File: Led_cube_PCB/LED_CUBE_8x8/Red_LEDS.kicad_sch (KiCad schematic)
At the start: 34 parts, among them IC16 74AHCT244PW,118, IC19 74AHCT244PW,118, IC20 74AHCT244PW,118, IC21 74AHCT244PW,118, IC22 74AHCT244PW,118, IC4 74AHCT244PW,118, IC5 74AHCT244PW,118, IC6 74AHCT244PW,118, IC7 74AHC138PW,118

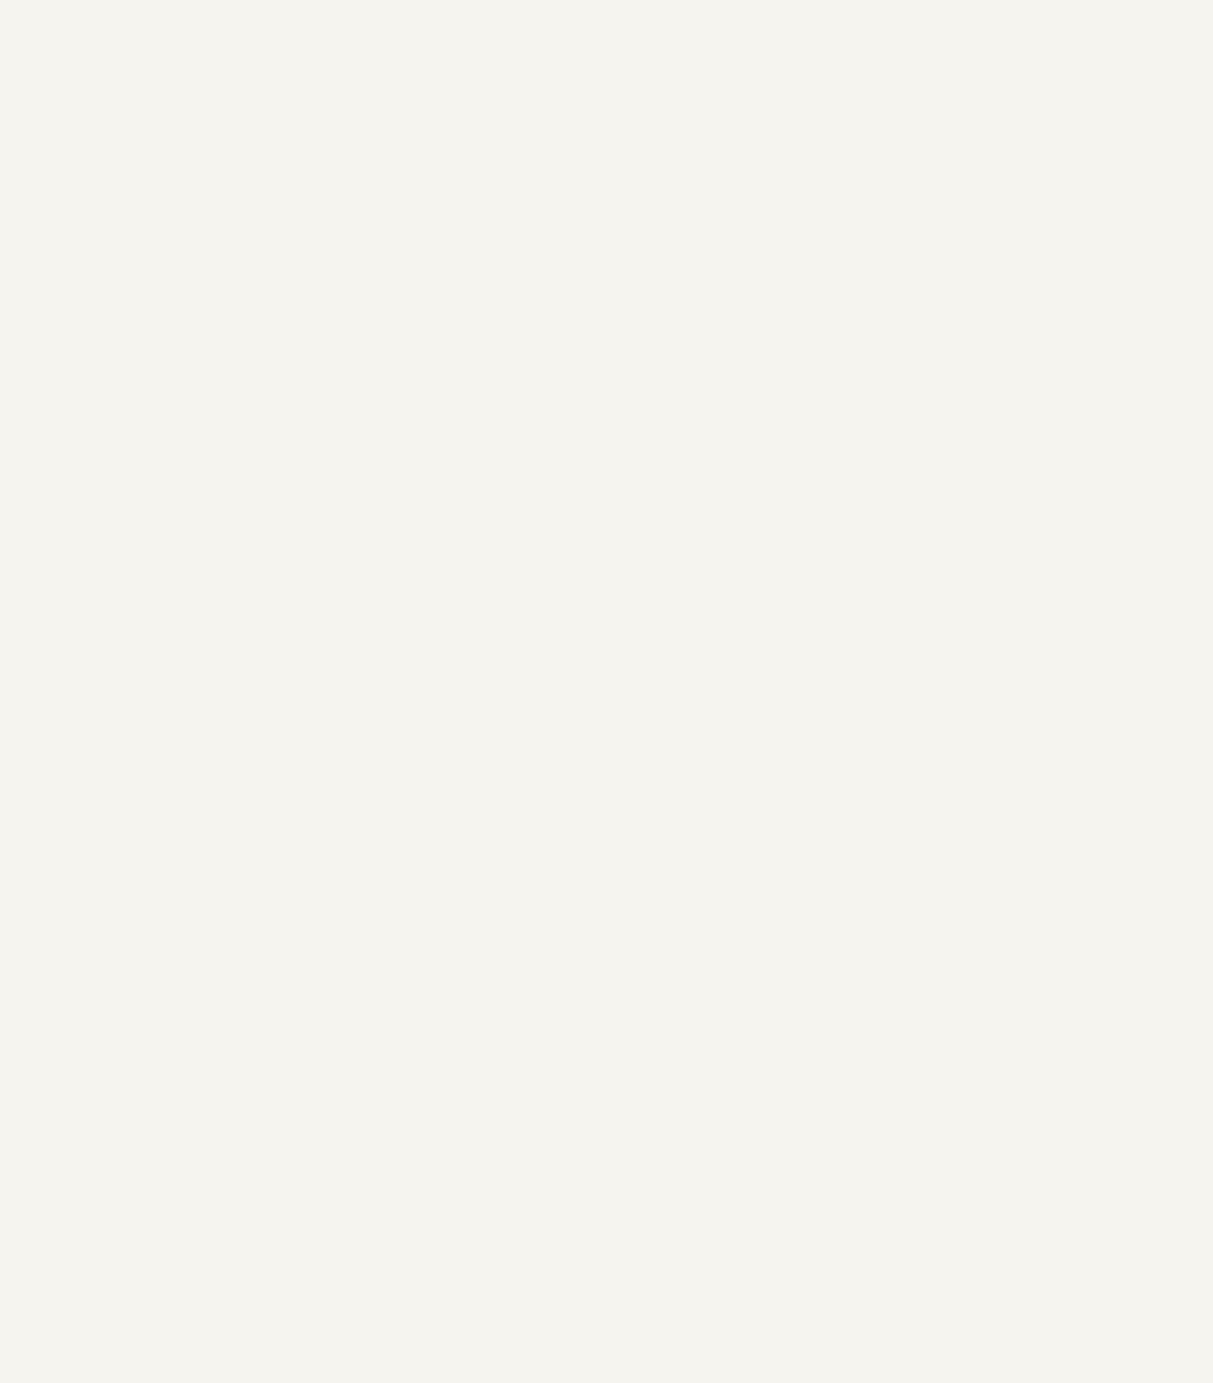
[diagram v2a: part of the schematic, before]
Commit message: added connector and current limiting resistors of the RED channel.
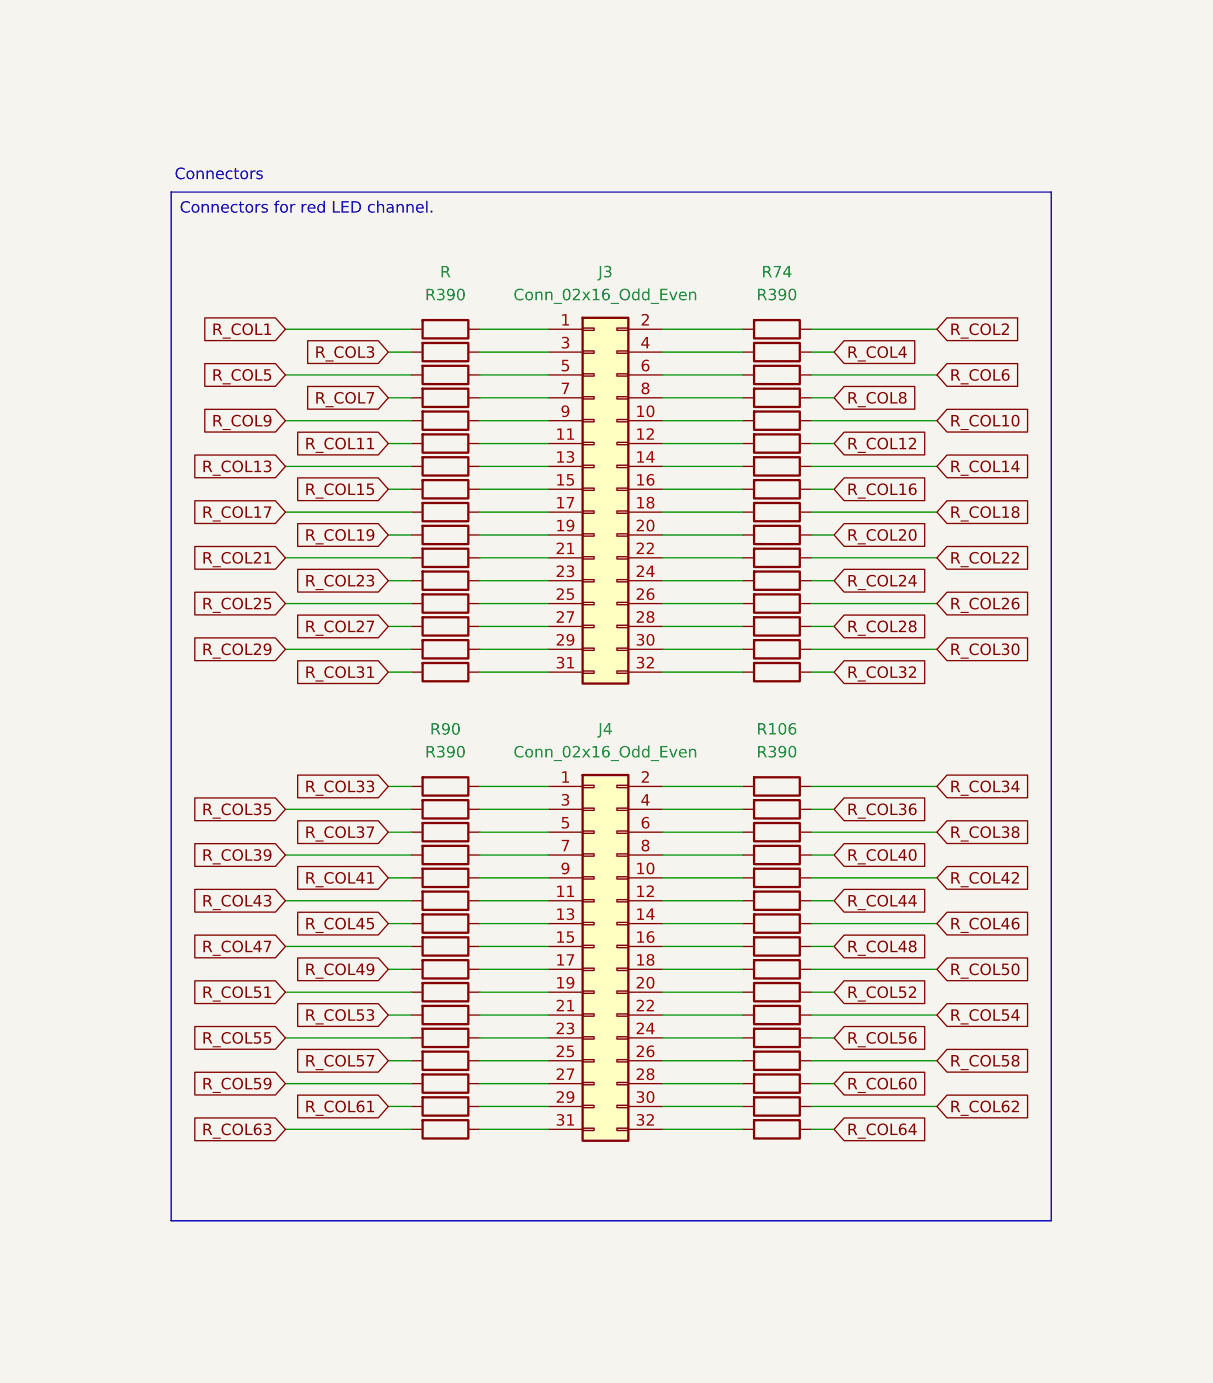
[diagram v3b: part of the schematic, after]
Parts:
- added J3, J4: Conn_02x16_Odd_Even, Connector_PinHeader_1.00mm:PinHeader_2x16_P1.00mm_Vertical, symbol Connector_Generic:Conn_02x16_Odd_Even
- added R (x2), R100, R101, R102, R103, R104, R105, R106, R107, R108, R109, R110, R111, R112, R113, R114, R115, R116, R117, R118, R119, R120, R121, R60, R61, R62, R63, R64, R65, R66, R67, R68, R69, R70, R71, R72, R73, R74, R75, R76, R77, R78, R79, R80, R81, R82, R83, R84, R85, R86, R87, R88, R89, R90, R91, R92, R93, R94, R95, R96, R97, R98, R99: R390, symbol Device:R
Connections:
- net R_COL1: now also R.2
- net R_COL10: now also R78.1
- net R_COL11: now also R63.2
- net R_COL12: now also R79.1
- net R_COL13: now also R64.2
- net R_COL14: now also R80.1
- net R_COL15: now also R65.2
- net R_COL16: now also R81.1
- net R_COL17: now also R66.2
- net R_COL18: now also R82.1
- net R_COL19: now also R67.2
- net R_COL2: now also R74.1
- net R_COL20: now also R83.1
- net R_COL21: now also R68.2
- net R_COL22: now also R84.1
- net R_COL23: now also R69.2
- net R_COL24: now also R85.1
- net R_COL25: now also R70.2
- net R_COL26: now also R86.1
- net R_COL27: now also R71.2
- net R_COL28: now also R87.1
- net R_COL29: now also R72.2
- net R_COL3: now also R.2
- net R_COL30: now also R88.1
- net R_COL31: now also R73.2
- net R_COL32: now also R89.1
- net R_COL33: now also R90.2
- net R_COL34: now also R106.1
- net R_COL35: now also R91.2
- net R_COL36: now also R107.1
- net R_COL37: now also R92.2
- net R_COL38: now also R108.1
- net R_COL39: now also R93.2
- net R_COL4: now also R75.1
- net R_COL40: now also R109.1
- net R_COL41: now also R94.2
- net R_COL42: now also R110.1
- net R_COL43: now also R95.2
- net R_COL44: now also R111.1
- net R_COL45: now also R96.2
- net R_COL46: now also R112.1
- net R_COL47: now also R97.2
- net R_COL48: now also R113.1
- net R_COL49: now also R98.2
- net R_COL5: now also R60.2
- net R_COL50: now also R114.1
- net R_COL51: now also R99.2
- net R_COL52: now also R115.1
- net R_COL53: now also R100.2
- net R_COL54: now also R116.1
- net R_COL55: now also R101.2
- net R_COL56: now also R117.1
- net R_COL57: now also R102.2
- net R_COL58: now also R118.1
- net R_COL59: now also R103.2
- net R_COL6: now also R76.1
- net R_COL60: now also R119.1
- net R_COL61: now also R104.2
- net R_COL62: now also R120.1
- net R_COL63: now also R105.2
- net R_COL64: now also R121.1
- net R_COL7: now also R61.2
- net R_COL8: now also R77.1
- net R_COL9: now also R62.2
- new net: J3.24 (Pin_24), R85.2
- new net: J3.32 (Pin_32), R89.2
- new net: J3.26 (Pin_26), R86.2
- new net: J4.11 (Pin_11), R95.1
- new net: J3.28 (Pin_28), R87.2
- new net: J4.16 (Pin_16), R113.2
- new net: J4.24 (Pin_24), R117.2
- new net: J4.29 (Pin_29), R104.1
- new net: J3.25 (Pin_25), R70.1
- new net: J4.26 (Pin_26), R118.2
- new net: J4.25 (Pin_25), R102.1
- new net: J4.23 (Pin_23), R101.1
- new net: J4.6 (Pin_6), R108.2
- new net: J3.20 (Pin_20), R83.2
- new net: J3.19 (Pin_19), R67.1
- new net: J3.14 (Pin_14), R80.2
- new net: J3.7 (Pin_7), R61.1
- new net: J4.10 (Pin_10), R110.2
- new net: J3.2 (Pin_2), R74.2
- new net: J4.32 (Pin_32), R121.2
- new net: J3.6 (Pin_6), R76.2
- new net: J4.9 (Pin_9), R94.1
- new net: J4.22 (Pin_22), R116.2
- new net: J4.27 (Pin_27), R103.1
- new net: J3.5 (Pin_5), R60.1
- new net: J3.10 (Pin_10), R78.2
- new net: J4.31 (Pin_31), R105.1
- new net: J4.3 (Pin_3), R91.1
- new net: J4.18 (Pin_18), R114.2
- new net: J3.22 (Pin_22), R84.2
- new net: J4.12 (Pin_12), R111.2
- new net: J4.17 (Pin_17), R98.1
- new net: J3.18 (Pin_18), R82.2
- new net: J3.9 (Pin_9), R62.1
- new net: J4.7 (Pin_7), R93.1
- new net: J3.15 (Pin_15), R65.1
- new net: J3.1 (Pin_1), R.1
- new net: J4.4 (Pin_4), R107.2
- new net: J3.21 (Pin_21), R68.1
- new net: J3.4 (Pin_4), R75.2
- new net: J3.8 (Pin_8), R77.2
- new net: J4.30 (Pin_30), R120.2
- new net: J3.11 (Pin_11), R63.1
- new net: J3.12 (Pin_12), R79.2
- new net: J3.13 (Pin_13), R64.1
- new net: J3.16 (Pin_16), R81.2
- new net: J3.17 (Pin_17), R66.1
- new net: J3.23 (Pin_23), R69.1
- new net: J3.27 (Pin_27), R71.1
- new net: J3.29 (Pin_29), R72.1
- new net: J3.3 (Pin_3), R.1
- new net: J3.30 (Pin_30), R88.2
- new net: J3.31 (Pin_31), R73.1
- new net: J4.15 (Pin_15), R97.1
- new net: J4.1 (Pin_1), R90.1
- new net: J4.13 (Pin_13), R96.1
- new net: J4.14 (Pin_14), R112.2
- new net: J4.19 (Pin_19), R99.1
- new net: J4.2 (Pin_2), R106.2
- new net: J4.20 (Pin_20), R115.2
- new net: J4.21 (Pin_21), R100.1
- new net: J4.28 (Pin_28), R119.2
- new net: J4.5 (Pin_5), R92.1
- new net: J4.8 (Pin_8), R109.2
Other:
- note added: "Connectors"

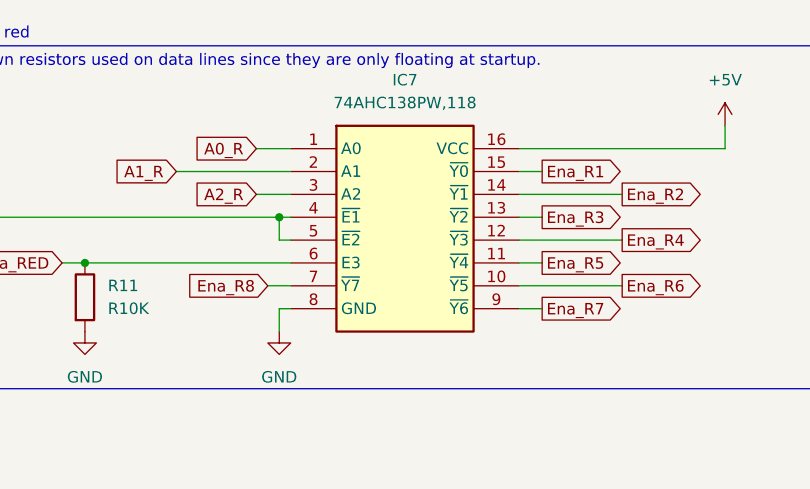
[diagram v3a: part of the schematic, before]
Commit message: added spice simulations folder, For simulating transients effect on the power buck converter. Also finished layer select in eeschema.
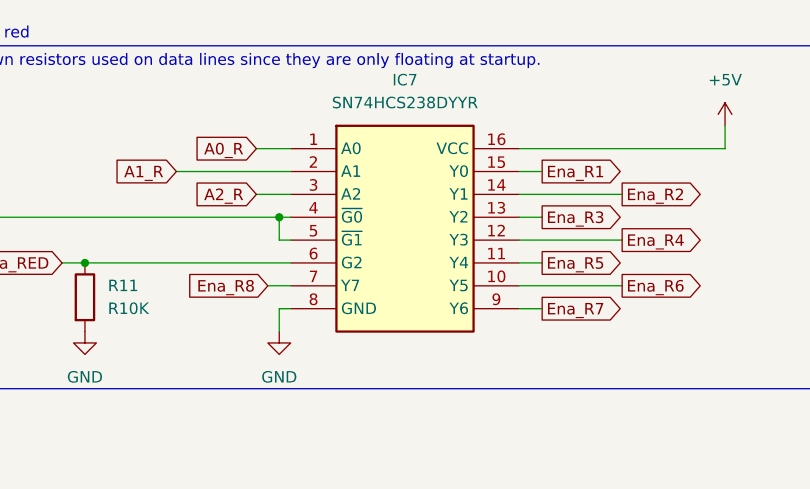
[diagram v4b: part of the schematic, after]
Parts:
- removed IC7: 74AHC138PW,118, SOP65P640X110-16N, symbol SamacSys_Parts:74AHC138PW,118
- added IC7: SN74HCS238DYYR, SOP50P326X110-16N, symbol SamacSys_Parts:SN74HCS238DYYR
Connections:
- net +5V: now also IC7.16 (VCC)
- net A0_R: now also IC7.1 (A0)
- net A1_R: now also IC7.2 (A1)
- net A2_R: now also IC7.3 (A2)
- net Ena_R1: now also IC7.15 (Y0)
- net Ena_R2: now also IC7.14 (Y1)
- net Ena_R3: now also IC7.13 (Y2)
- net Ena_R4: now also IC7.12 (Y3)
- net Ena_R5: now also IC7.11 (Y4)
- net Ena_R6: now also IC7.10 (Y5)
- net Ena_R7: now also IC7.9 (Y6)
- net Ena_R8: now also IC7.7 (Y7)
- net Ena_RED: now also IC7.6 (G2)
- net GND: now also IC7.4 (~{G0}), IC7.5 (~{G1}), IC7.8 (GND)
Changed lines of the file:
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@@
 	)
 	(symbol
+		(lib_id "SamacSys_Parts:SN74HCS238DYYR")
+		(at 335.28 27.94 0)
+		(unit 1)
+		(exclude_from_sim no)
+		(in_bom yes)
+		(on_board yes)
+		(dnp no)
+		(fields_autoplaced yes)
+		(property "Reference" "IC7"
+			(at 347.98 20.32 0)
+			(effects
+				(font
+					(size 1.27 1.27)
+				)
+			)
+		)
+		(property "Value" "SN74HCS238DYYR"
+			(at 347.98 22.86 0)
+			(effects
+				(font
+					(size 1.27 1.27)
+				)
+			)
+		)
+		(property "Footprint" "SOP50P326X110-16N"
+			(at 356.87 122.86 0)
+			(effects
+				(font
+					(size 1.27 1.27)
+				)
+				(justify left top)
+				(hide yes)
+			)
+		)
+		(property "Datasheet" "https://www.ti.com/general/docs/suppproductinfo.tsp?distId=26&gotoUrl=https://www.ti.com/lit/gpn/sn74hcs238"
+			(at 356.87 222.86 0)
+			(effects
+				(font
+					(size 1.27 1.27)
+				)
+				(justify left top)
+				(hide yes)
+			)
+		)
+		(property "Description" "3-To-8 Line Decoder Demultiplexer Inverting And Non-Inverting With Schmitt-Trigger Input"
+			(at 335.28 27.94 0)
+			(effects
+				(font
+					(size 1.27 1.27)
+				)
+				(hide yes)
+			)
+		)
+		(property "Height" "1.1"
+			(at 356.87 422.86 0)
+			(effects
+				(font
+					(size 1.27 1.27)
+				)
+				(justify left top)
+				(hide yes)
+			)
+		)
+		(property "Mouser Part Number" "595-SN74HCS238DYYR"
+			(at 356.87 522.86 0)
+			(effects
+				(font
+					(size 1.27 1.27)
+				)
+				(justify left top)
+				(hide yes)
+			)
+		)
+		(property "Mouser Price/Stock" "https://www.mouser.co.uk/ProductDetail/Texas-Instruments/SN74HCS238DYYR?qs=QNEnbhJQKvaif85BFm1rOg%3D%3D"
+			(at 356.87 622.86 0)
+			(effects
+				(font
+					(size 1.27 1.27)
+				)
+				(justify left top)
+				(hide yes)
+			)
+		)
+		(property "Manufacturer_Name" "Texas Instruments"
+			(at 356.87 722.86 0)
+			(effects
+				(font
+					(size 1.27 1.27)
+				)
+				(justify left top)
+				(hide yes)
+			)
+		)
+		(property "Manufacturer_Part_Number" "SN74HCS238DYYR"
+			(at 356.87 822.86 0)
+			(effects
+				(font
+					(size 1.27 1.27)
+				)
+				(justify left top)
+				(hide yes)
+			)
+		)
+		(pin "13"
+		)
+		(pin "6"
+		)
+		(pin "7"
+		)
+		(pin "4"
+		)
+		(pin "16"
+		)
+		(pin "2"
+		)
+		(pin "1"
+		)
+		(pin "9"
+		)
+		(pin "8"
+		)
+		(pin "3"
+		)
+		(pin "15"
+		)
+		(pin "14"
+		)
+		(pin "12"
+		)
+		(pin "11"
+		)
+		(pin "5"
+		)
+		(pin "10"
+		)
+		(instances
+			(project ""
+				(path "/b239677e-e361-4439-8200-63fb41f7e03c/39f84ab9-cf03-4ef5-a6b6-c3023701b456"
+					(reference "IC7")
+					(unit 1)
+				)
+			)
+		)
+	)
+	(symbol
 		(lib_id "Device:R")
 		(at 355.6 123.19 270)
@@
 					(unit 1)
 				)
-			)
-		)
-	)
-	(symbol
-		(lib_id "SamacSys_Parts:74AHC138PW,118")
-		(at 335.28 27.94 0)
-		(unit 1)
-		(exclude_from_sim no)
-		(in_bom yes)
-		(on_board yes)
-		(dnp no)
-		(fields_autoplaced yes)
-		(property "Reference" "IC7"
-			(at 347.98 20.32 0)
-			(effects
-				(font
-					(size 1.27 1.27)
-				)
-			)
-		)
-		(property "Value" "74AHC138PW,118"
-			(at 347.98 22.86 0)
-			(effects
-				(font
-					(size 1.27 1.27)
-				)
-			)
-		)
-		(property "Footprint" "SOP65P640X110-16N"
-			(at 356.87 122.86 0)
-			(effects
-				(font
-					(size 1.27 1.27)
-				)
-				(justify left top)
-				(hide yes)
-			)
-		)
-		(property "Datasheet" "https://componentsearchengine.com/Datasheets/1/74AHC138PW,118.pdf"
-			(at 356.87 222.86 0)
-			(effects
-				(font
-					(size 1.27 1.27)
-				)
-				(justify left top)
-				(hide yes)
-			)
-		)
-		(property "Description" "74AHC(T)138 - 3-to-8 line decoder/demultiplexer; inverting@en-us"
-			(at 335.28 27.94 0)
-			(effects
-				(font
-					(size 1.27 1.27)
-				)
-				(hide yes)
-			)
-		)
-		(property "Height" "1.1"
-			(at 356.87 422.86 0)
-			(effects
-				(font
-					(size 1.27 1.27)
-				)
-				(justify left top)
-				(hide yes)
-			)
-		)
-		(property "Mouser Part Number" "771-AHC138PW118"
-			(at 356.87 522.86 0)
-			(effects
-				(font
-					(size 1.27 1.27)
-				)
-				(justify left top)
-				(hide yes)
-			)
-		)
-		(property "Mouser Price/Stock" "https://www.mouser.com/Search/Refine.aspx?Keyword=771-AHC138PW118"
-			(at 356.87 622.86 0)
-			(effects
-				(font
-					(size 1.27 1.27)
-				)
-				(justify left top)
-				(hide yes)
-			)
-		)
-		(property "Manufacturer_Name" "Nexperia"
-			(at 356.87 722.86 0)
-			(effects
-				(font
-					(size 1.27 1.27)
-				)
-				(justify left top)
-				(hide yes)
-			)
-		)
-		(property "Manufacturer_Part_Number" "74AHC138PW,118"
-			(at 356.87 822.86 0)
-			(effects
-				(font
-					(size 1.27 1.27)
-				)
-				(justify left top)
-				(hide yes)
-			)
-		)
-		(pin "4"
-		)
-		(pin "15"
-		)
-		(pin "2"
-		)
-		(pin "7"
-		)
-		(pin "12"
-		)
-		(pin "1"
-		)
-		(pin "11"
-		)
-		(pin "10"
-		)
-		(pin "8"
-		)
-		(pin "16"
-		)
-		(pin "9"
-		)
-		(pin "3"
-		)
-		(pin "13"
-		)
-		(pin "5"
-		)
-		(pin "6"
-		)
-		(pin "14"
-		)
-		(instances
-			(project "LED_CUBE_8x8"
-				(path "/b239677e-e361-4439-8200-63fb41f7e03c/39f84ab9-cf03-4ef5-a6b6-c3023701b456"
-					(reference "IC7")
-					(unit 1)
-				)
